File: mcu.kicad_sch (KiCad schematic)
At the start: 27 parts, among them J17 CAN, J19 Conn_ARM_JTAG_SWD_10, SW1 RESET, U17 HDC1080, U18 SN65HVD230, U8 STM32G431CBTx, Y1 8 MHz

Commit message: Add title to all schematics pages
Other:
- title: (none) -> MCU
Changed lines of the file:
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@@
 	(paper "A4")
 	(title_block
+		(title "MCU")
 		(rev "1")
 	)

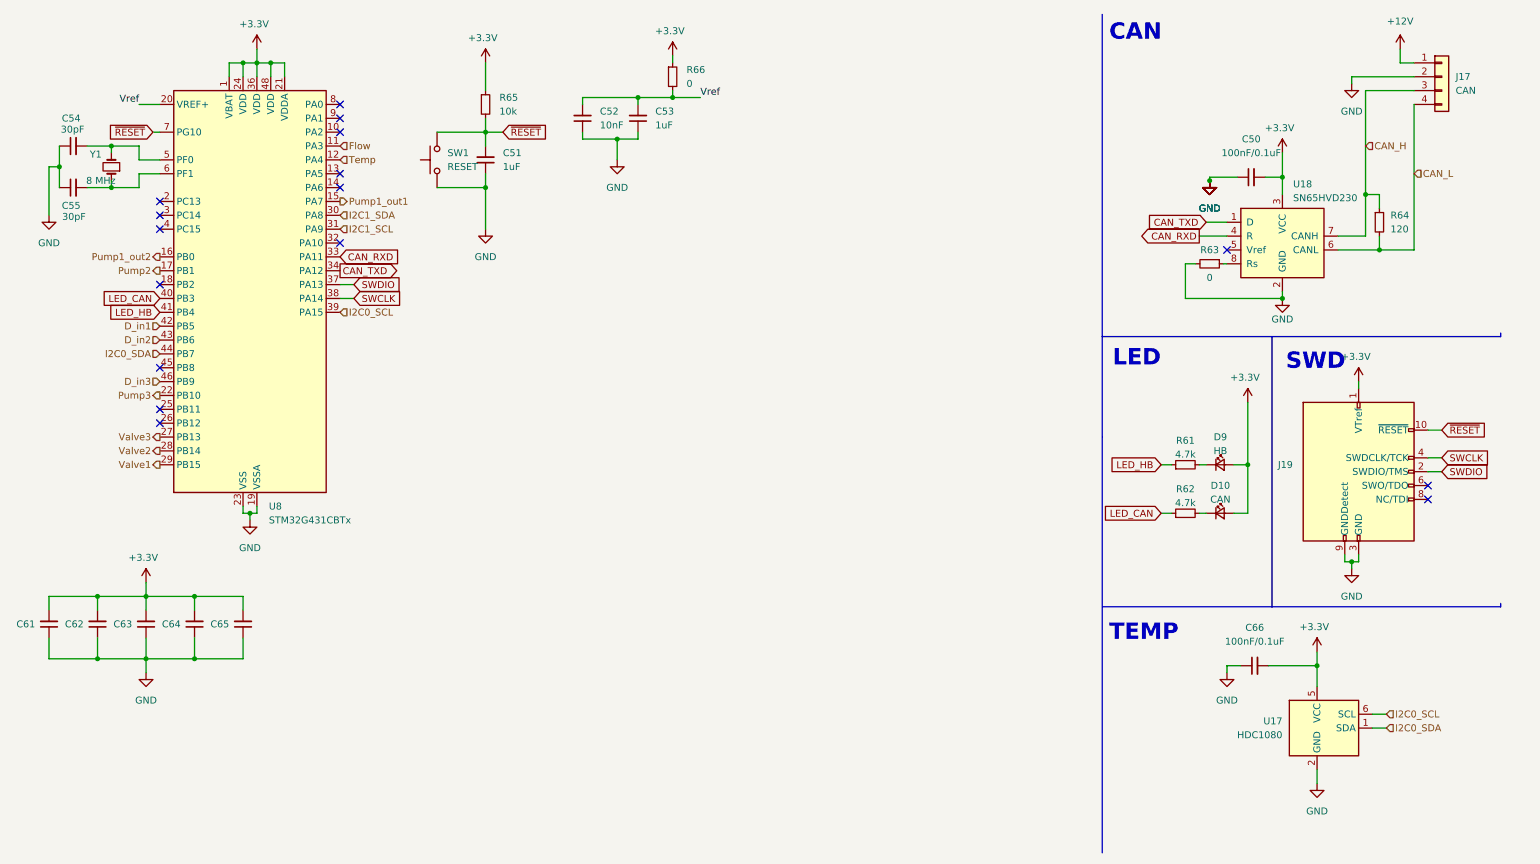
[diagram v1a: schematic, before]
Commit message: Redesign board to fit within 102mm x 102mm
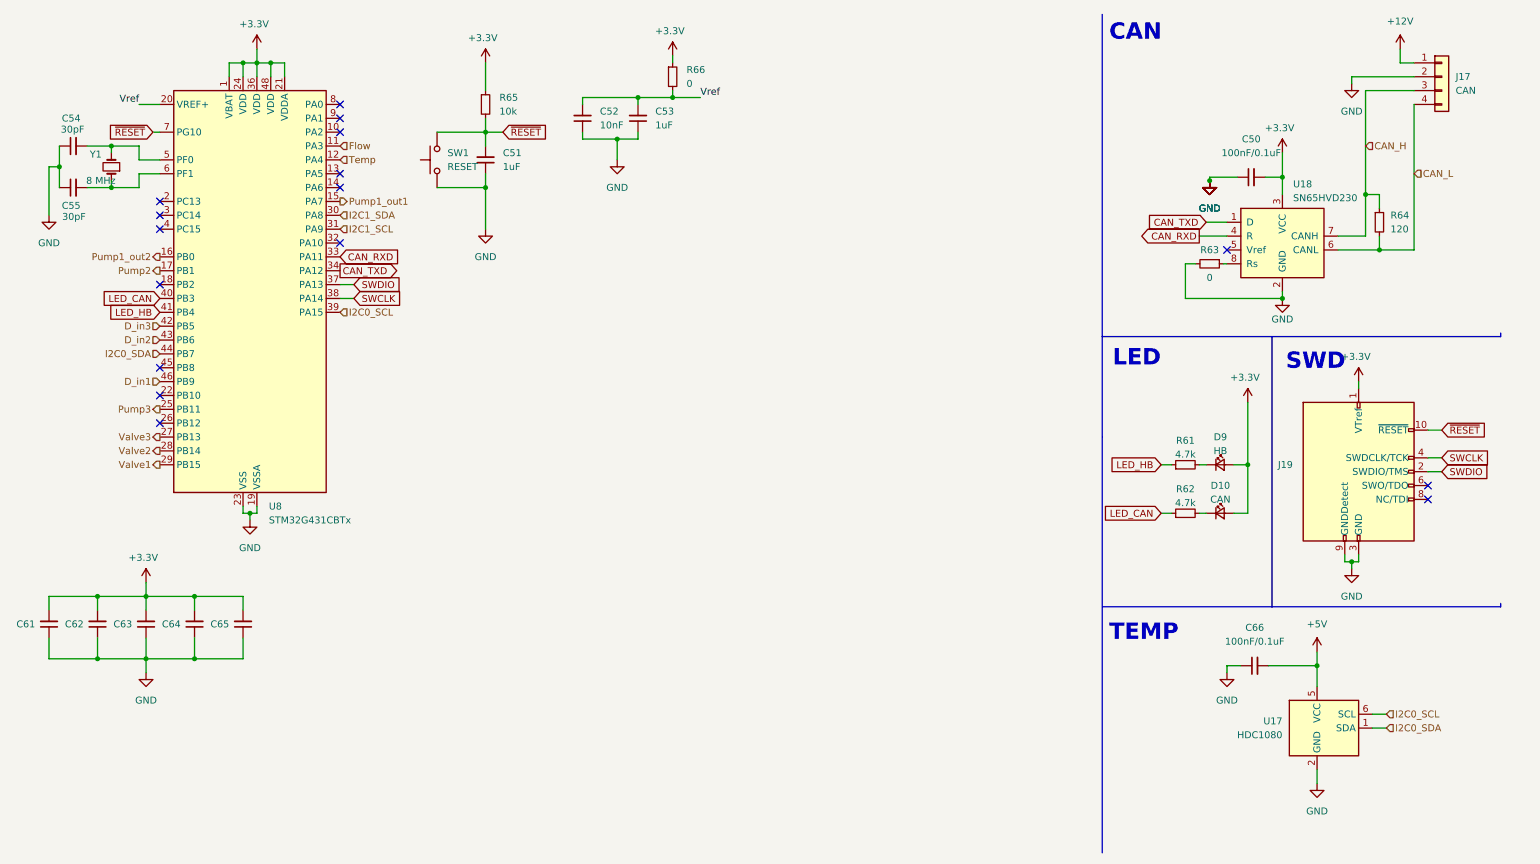
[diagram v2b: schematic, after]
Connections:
- net +3.3V: no longer C66.2, U17.5 (VCC)
- net D_in1: now also U8.46 (PB9); no longer U8.42 (PB5)
- net D_in3: now also U8.42 (PB5); no longer U8.46 (PB9)
- net Pump3: now also U8.25 (PB11); no longer U8.22 (PB10)
- new net +5V: C66.2, U17.5 (VCC)
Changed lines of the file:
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@@
 	)
 	(no_connect
-		(at 39.37 85.09)
+		(at 39.37 82.55)
 	)
 	(wire
@@
 		)
 	)
-	(hierarchical_label "D_in1"
+	(hierarchical_label "D_in3"
 		(shape input)
 		(at 39.37 69.85 180)
@@
 		)
 	)
-	(hierarchical_label "D_in3"
+	(hierarchical_label "D_in1"
 		(shape input)
 		(at 39.37 80.01 180)
@@
 	(hierarchical_label "Pump3"
 		(shape output)
-		(at 39.37 82.55 180)
+		(at 39.37 85.09 180)
 		(fields_autoplaced yes)
 		(effects
@@
 	(symbol
 		(lib_id "power:+3.3V")
-		(at 251.46 129.54 0)
-		(unit 1)
-		(exclude_from_sim no)
-		(in_bom yes)
-		(on_board yes)
-		(dnp no)
-		(property "Reference" "#PWR0150"
-			(at 251.46 133.35 0)
-			(effects
-				(font
-					(size 1.27 1.27)
-				)
-				(hide yes)
-			)
-		)
-		(property "Value" "+3.3V"
-			(at 250.952 124.968 0)
-			(effects
-				(font
-					(size 1.27 1.27)
-				)
-			)
-		)
-		(property "Footprint" ""
-			(at 251.46 129.54 0)
-			(effects
-				(font
-					(size 1.27 1.27)
-				)
-				(hide yes)
-			)
-		)
-		(property "Datasheet" ""
-			(at 251.46 129.54 0)
-			(effects
-				(font
-					(size 1.27 1.27)
-				)
-				(hide yes)
-			)
-		)
-		(property "Description" "Power symbol creates a global label with name \"+3.3V\""
-			(at 251.46 129.54 0)
-			(effects
-				(font
-					(size 1.27 1.27)
-				)
-				(hide yes)
-			)
-		)
-		(pin "1"
-		)
-		(instances
-			(project "HydroponicFlowerControl"
-				(path "/b3c8a28b-9ce1-4002-b8e8-ef8cb73fe031/ed65d457-d819-4893-a974-b640bac4c870"
-					(reference "#PWR0150")
-					(unit 1)
-				)
-			)
-		)
-	)
-	(symbol
-		(lib_id "power:+3.3V")
 		(at 57.15 19.05 0)
 		(unit 1)
@@
 		)
 		(property "Value" "100nF/0.1uF"
-			(at 51.562 113.538 90)
+			(at 69.596 127.254 0)
 			(effects
 				(font
@@
 					(unit 1)
 				)
+			)
+		)
+	)
+	(symbol
+		(lib_id "power:+5V")
+		(at 251.46 129.54 0)
+		(unit 1)
+		(exclude_from_sim no)
+		(in_bom yes)
+		(on_board yes)
+		(dnp no)
+		(fields_autoplaced yes)
+		(property "Reference" "#PWR0153"
+			(at 251.46 133.35 0)
+			(effects
+				(font
+					(size 1.27 1.27)
+				)
+				(hide yes)
+			)
+		)
+		(property "Value" "+5V"
+			(at 251.46 124.46 0)
+			(effects
+				(font
+					(size 1.27 1.27)
+				)
+			)
+		)
+		(property "Footprint" ""
+			(at 251.46 129.54 0)
+			(effects
+				(font
+					(size 1.27 1.27)
+				)
+				(hide yes)
+			)
+		)
+		(property "Datasheet" ""
+			(at 251.46 129.54 0)
+			(effects
+				(font
+					(size 1.27 1.27)
+				)
+				(hide yes)
+			)
+		)
+		(property "Description" "Power symbol creates a global label with name \"+5V\""
+			(at 251.46 129.54 0)
+			(effects
+				(font
+					(size 1.27 1.27)
+				)
+				(hide yes)
+			)
+		)
+		(pin "1"
+		)
+		(instances
+			(project "HydroponicFlowerControl"
+				(path "/b3c8a28b-9ce1-4002-b8e8-ef8cb73fe031/ed65d457-d819-4893-a974-b640bac4c870"
+					(reference "#PWR0153")
+					(unit 1)
+				)

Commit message: Add revision resistors
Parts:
- added R70, R71, R72, R73, R74, R75: 10k, Resistor_SMD:R_0402_1005Metric, symbol Device:R_Small
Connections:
- net +3.3V: now also R70.1, R72.1, R74.1
- net GND: now also R71.2, R73.2, R75.2
- net HW_rev2: now reaches U8.10 (PA2)
- net HW_rev2: now also R70.2, R71.1
- net HW_rev0: now reaches U8.8 (PA0)
- net HW_rev0: now also R74.2, R75.1
- net HW_rev1: now reaches U8.9 (PA1)
- net HW_rev1: now also R72.2, R73.1
- no-connect marks 16 -> 13
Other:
- note added: "HW rev"

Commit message: Add disable signals for ec and ph
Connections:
- net ec_disable: now reaches U8.2 (PC13)
- net pH_disable: now reaches U8.3 (PC14)
- no-connect marks 13 -> 11
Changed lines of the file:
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@@
-	)
-	(no_connect
-		(at 39.37 49.53)
 	)
 	(no_connect
@@
 	(no_connect
 		(at 39.37 87.63)
-	)
-	(no_connect
-		(at 39.37 46.99)
 	)
 	(no_connect
@@
 		)
 	)
+	(hierarchical_label "ec_disable"
+		(shape output)
+		(at 39.37 46.99 180)
+		(fields_autoplaced yes)
+		(effects
+			(font
+				(size 1.27 1.27)
+			)
+			(justify right)
+		)
+	)
 	(hierarchical_label "I2C0_SDA"
 		(shape input)
@@
 		)
 	)
+	(hierarchical_label "pH_disable"
+		(shape output)
+		(at 39.37 49.53 180)
+		(fields_autoplaced yes)
+		(effects
+			(font
+				(size 1.27 1.27)
+			)
+			(justify right)
+		)
+	)

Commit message: Update production data
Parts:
- J17: now left out of the parts list
- U18: JLCPCB Rotation Offset -90 -> 0
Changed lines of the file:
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@@
 			)
 		)
-		(property "JLCPCB Rotation Offset" "-90"
+		(property "JLCPCB Rotation Offset" "0"
 			(at 245.11 53.34 0)
 			(effects
@@
 		(unit 1)
 		(exclude_from_sim no)
-		(in_bom yes)
+		(in_bom no)
 		(on_board yes)
 		(dnp no)

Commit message: Replace motor controller with mosfets instead
Closes #21
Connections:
- net Pump1_out1 renamed Pump1
- net Pump1_out2: no longer names the net of U8.16 (PB0)
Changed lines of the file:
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@@
 		)
 	)
-	(hierarchical_label "Pump1_out1"
+	(hierarchical_label "Pump1"
 		(shape output)
 		(at 72.39 46.99 0)
@@
 		(fields_autoplaced yes)
 		(effects
-			(font
-				(size 1.27 1.27)
-			)
-			(justify right)
-		)
-	)
-	(hierarchical_label "Pump1_out2"
-		(shape output)
-		(at 39.37 57.15 180)
-		(fields_autoplaced yes)
-		(effects

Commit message: Add Cortex debug connector
Closes #17
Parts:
- added J20: Conn_ARM_JTAG_SWD_10, Connector_PinHeader_1.27mm:PinHeader_2x05_P1.27mm_Vertical_SMD, symbol Connector:Conn_ARM_JTAG_SWD_10
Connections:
- net +3.3V: now also J20.1 (VTref)
- net GND: now also J20.3 (GND), J20.5 (GND), J20.9 (GNDDetect)
- net SWCLK: now also J20.4 (SWDCLK/TCK)
- net SWDIO: now also J20.2 (SWDIO/TMS)
- net ~{RESET}: now also J20.10 (~{RESET})
- no-connect marks 11 -> 13
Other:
- note added: "Cortex debug"
- note added: "TagConnect"
- moved on the sheet: D10, D9, J19, R61, R62

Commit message: Tie boot0 (PB8) to GND
Closes #2
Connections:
- net GND: now also U8.45 (PB8)
- no-connect marks 13 -> 12
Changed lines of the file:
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@@
 	)
 	(no_connect
-		(at 39.37 77.47)
-	)
-	(no_connect
 		(at 276.86 101.6)
 	)
@@
 	(wire
 		(pts
+			(xy 24.13 77.47) (xy 39.37 77.47)
+		)
+		(stroke
+			(width 0)
+			(type default)
+		)
+	)
+	(wire
+		(pts
 			(xy 26.035 36.83) (xy 30.48 36.83)
 		)
@@
 	(wire
 		(pts
+			(xy 24.13 80.01) (xy 24.13 77.47)
+		)
+		(stroke
+			(width 0)
+			(type default)
+		)
+	)
+	(wire
+		(pts
 			(xy 255.27 55.88) (xy 262.89 55.88)
 		)
@@
 					(unit 1)
 				)
+			)
+		)
+	)
+	(symbol
+		(lib_id "power:GND")
+		(at 24.13 80.01 0)
+		(unit 1)
+		(exclude_from_sim no)
+		(in_bom yes)
+		(on_board yes)
+		(dnp no)
+		(fields_autoplaced yes)
+		(property "Reference" "#PWR032"
+			(at 24.13 86.36 0)
+			(effects
+				(font
+					(size 1.27 1.27)
+				)
+				(hide yes)
+			)
+		)
+		(property "Value" "GND"
+			(at 24.13 85.09 0)
+			(effects
+				(font
+					(size 1.27 1.27)
+				)
+			)
+		)
+		(property "Footprint" ""
+			(at 24.13 80.01 0)
+			(effects
+				(font
+					(size 1.27 1.27)
+				)
+				(hide yes)
+			)
+		)
+		(property "Datasheet" ""
+			(at 24.13 80.01 0)
+			(effects
+				(font
+					(size 1.27 1.27)
+				)
+				(hide yes)
+			)
+		)
+		(property "Description" ""
+			(at 24.13 80.01 0)
+			(effects
+				(font
+					(size 1.27 1.27)
+				)
+				(hide yes)
+			)
+		)
+		(pin "1"
+		)
+		(instances
+			(project "HydroponicFlowerControl"
+				(path "/b3c8a28b-9ce1-4002-b8e8-ef8cb73fe031/ed65d457-d819-4893-a974-b640bac4c870"
+					(reference "#PWR032")
+					(unit 1)
+				)
